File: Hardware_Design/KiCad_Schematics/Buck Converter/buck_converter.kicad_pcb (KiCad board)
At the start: 2 copper layers, 42 x 22 mm, 9 parts, among them J1 Conn_01x02_Socket, J2 Conn_01x02_Socket, J3 Conn_01x01_Pin, Q1 2N7002

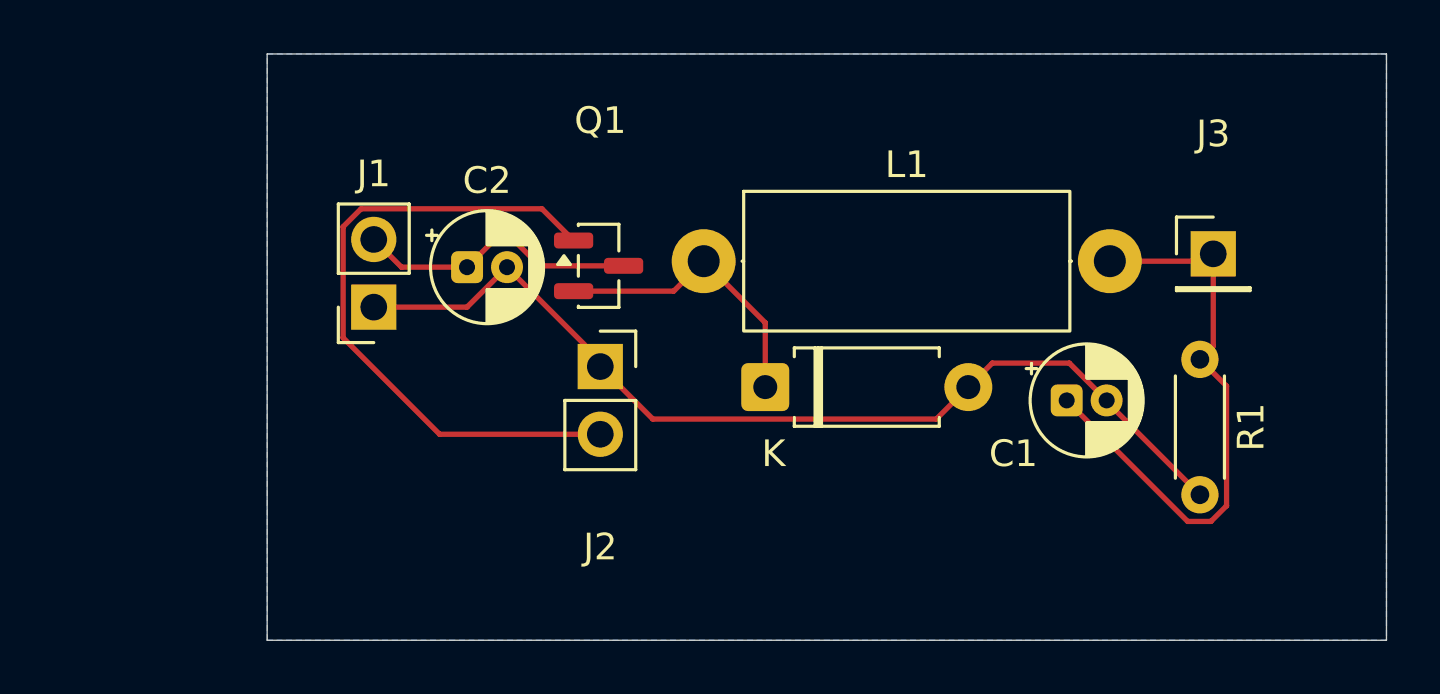
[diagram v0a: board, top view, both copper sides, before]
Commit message: refactor: update PCB layout and add 3D view
Change footprints for resistors, capacitors, and inductors. Refactor the design. Add 3D PCB view.
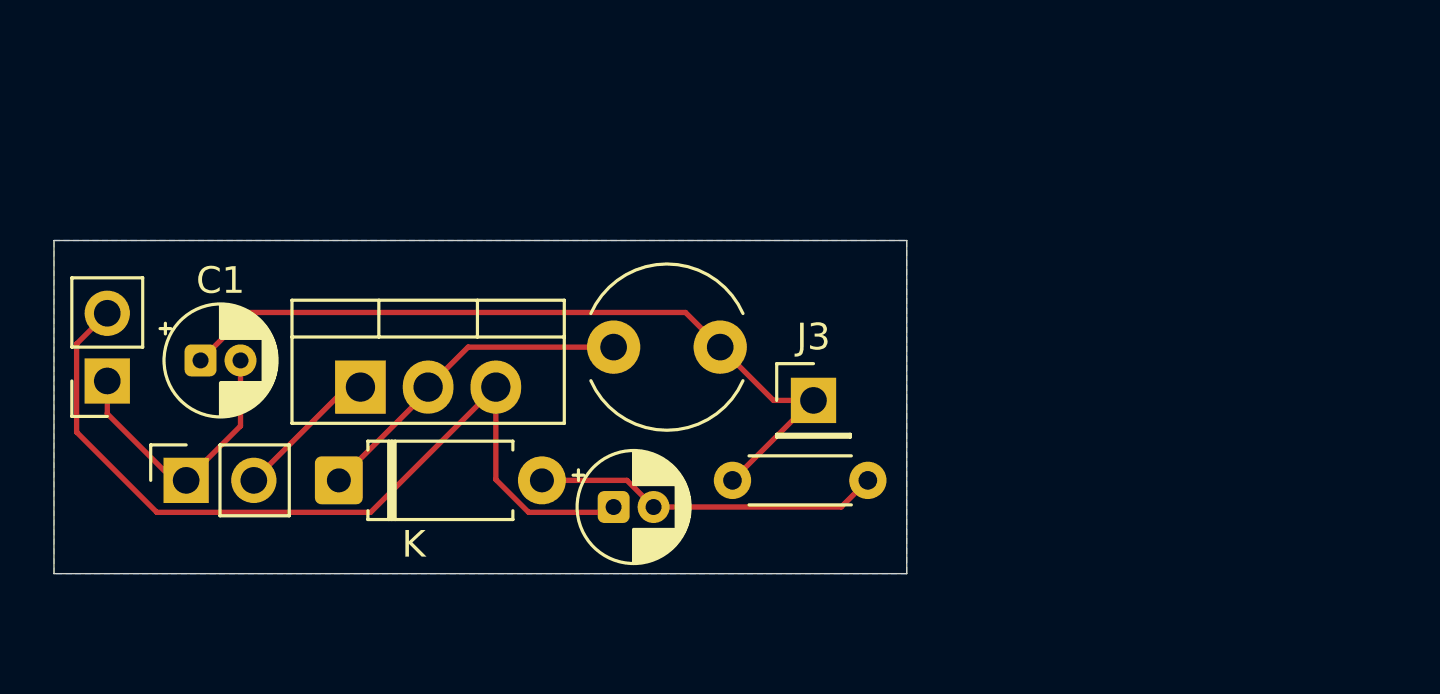
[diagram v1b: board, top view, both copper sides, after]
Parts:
- L1: footprint Inductor_THT:L_Axial_L12.0mm_D5.0mm_P15.24mm_Horizontal_Fastron_MISC -> Inductor_THT:L_Radial_D6.0mm_P4.00mm
- Q1: footprint Package_TO_SOT_SMD:SOT-23 -> Package_TO_SOT_THT:TO-220-3_Vertical
- moved C1 32.5 mm to (110.5, 99.5)
- moved R1 18.1 mm to (130.5, 104.0), turned to 0 degrees
- moved D1 16.4 mm to (115.7, 104.0)
- moved J2 16.1 mm to (110.0, 104.0), turned to 90 degrees
- moved J3 16.0 mm to (133.5, 101.0)
- moved C2 10.5 mm to (126.0, 105.0)
- moved J1 10.4 mm to (107.0, 100.3)
- moved Q1 10.0 mm to (116.5, 100.5)
- moved L1 4.67 mm to (126.0, 99.0)
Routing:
- net /DC: track 10.5 -> 32.3 mm
- net /PULSE: track 24.7 -> 5.45 mm
- net /GND: track 37.1 -> 23.6 mm
- net /OUTPUT: track 22.2 -> 29.4 mm
- net Net-(D1-K): track 11.0 -> 12.5 mm
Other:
- board size 42 x 22 mm -> 32 x 12.5 mm
